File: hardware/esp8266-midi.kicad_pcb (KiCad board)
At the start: 2 copper layers, 60.1 x 63.5 mm, 26 parts, among them J1 MIDI in, J2 MIDI out, J3 TTL-232R-3V3 connector, J4 Bat+, J5 Bat-, SW1 reset, SW2 prog enable, U1 ESP-12E, U2 6N138, U3 LD1117S50TR_SOT223

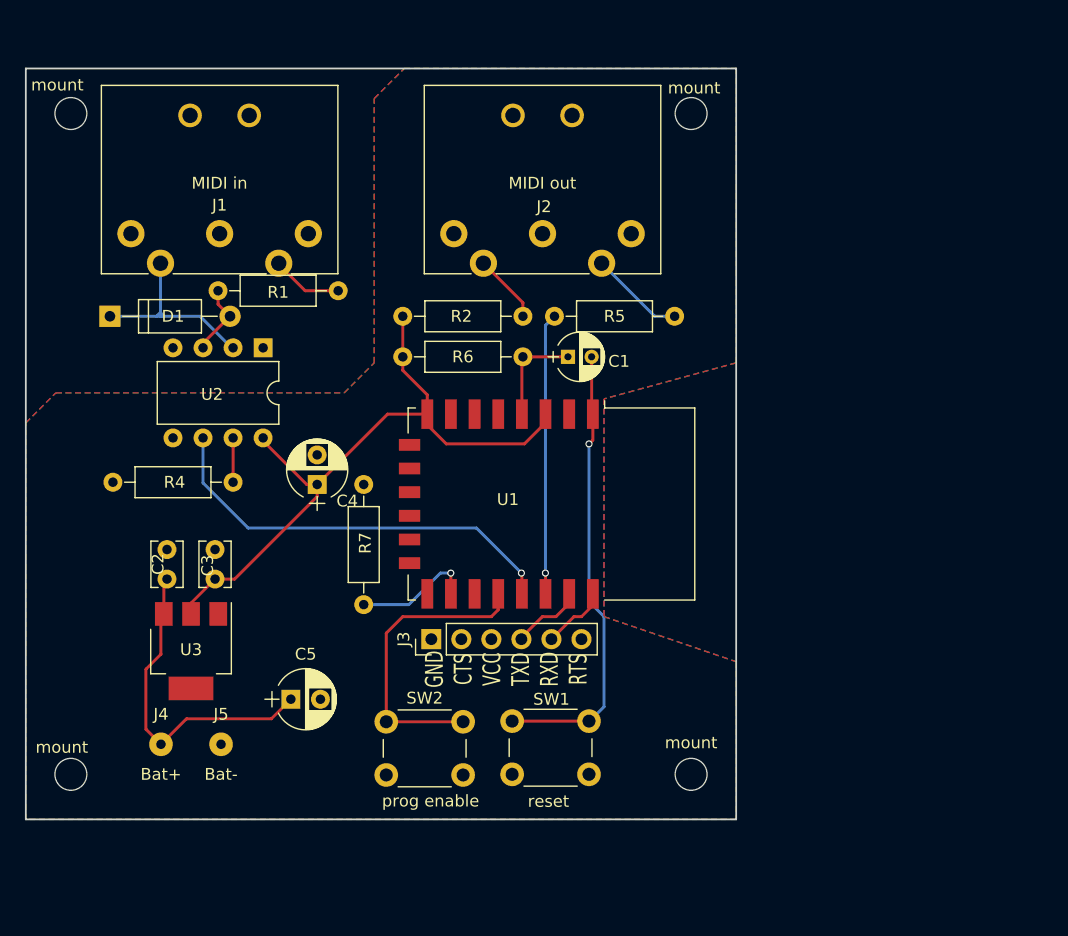
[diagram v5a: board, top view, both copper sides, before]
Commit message: New layout with (mostly) smd components, pcb shaped for CRDCGG003 enclosure
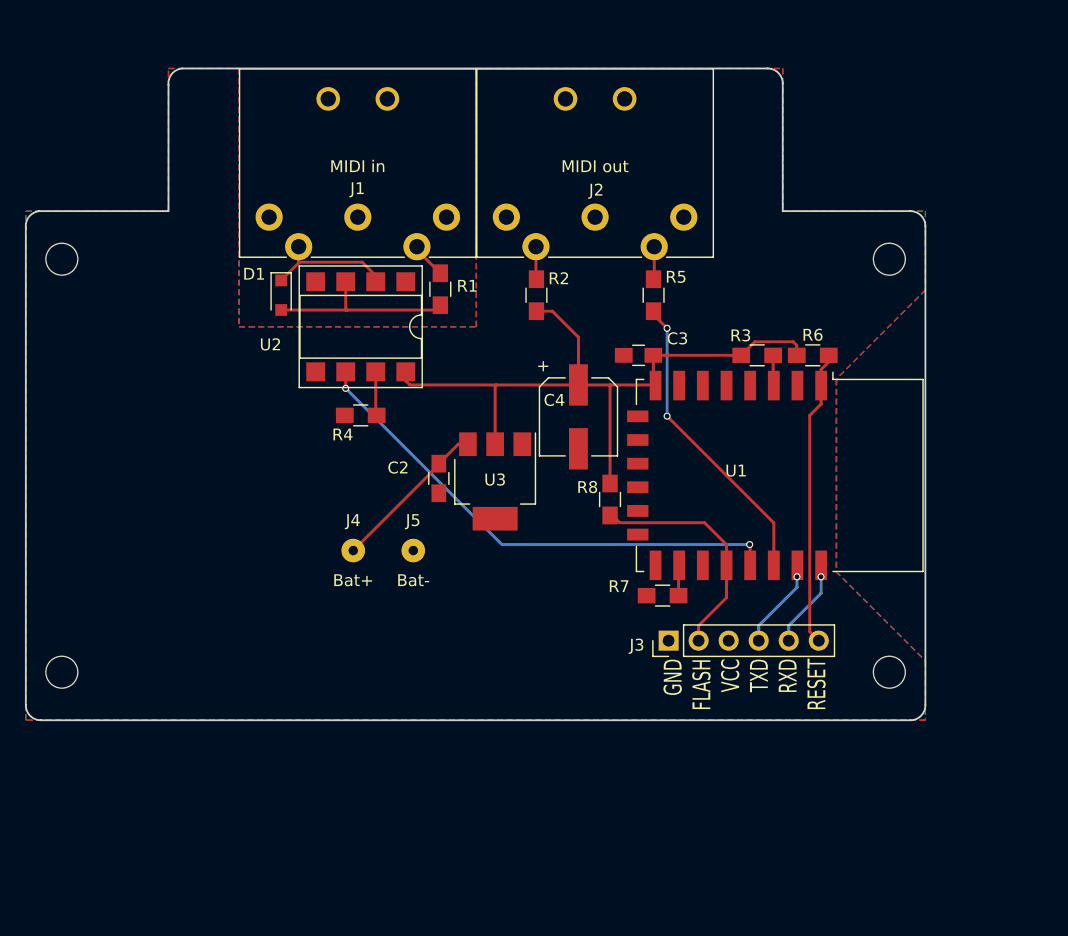
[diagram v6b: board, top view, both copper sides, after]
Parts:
- removed C1: 1uF, Capacitors_THT:CP_Radial_D4.0mm_P2.00mm
- removed C5: 220uF, Capacitors_THT:CP_Radial_D5.0mm_P2.50mm
- removed SW1: reset, Buttons_Switches_THT:SW_PUSH_6mm
- removed SW2: prog enable, Buttons_Switches_THT:SW_PUSH_6mm
- removed mount (x4): M2.5, Mounting_Holes:MountingHole_2.7mm_M2.5
- added ?: , Mounting_Holes:MountingHole_2.7mm_M2.5, F.Cu at (178.4, 120.3)
- added ?: , Mounting_Holes:MountingHole_2.7mm_M2.5, F.Cu at (178.4, 85.3)
- added ?: , Mounting_Holes:MountingHole_2.7mm_M2.5, F.Cu at (108.5, 120.3)
- added ?: , Mounting_Holes:MountingHole_2.7mm_M2.5, F.Cu at (108.5, 85.3)
- added R3: 10K, Resistors_SMD:R_0805_HandSoldering, F.Cu at (167.3, 93.5)
- added R8: 10K, Resistors_SMD:R_0805_HandSoldering, F.Cu at (154.8, 105.7)
- C2, C3: footprint Capacitors_THT:C_Disc_D3.8mm_W2.6mm_P2.50mm -> Capacitors_SMD:C_0805_HandSoldering
- C4: footprint Capacitors_THT:CP_Radial_D5.0mm_P2.50mm -> Capacitors_SMD:CP_Elec_6.3x5.8
- D1: footprint Diodes_THT:D_A-405_P10.16mm_Horizontal -> Diodes_SMD:D_SOD-323_HandSoldering
- R1, R2, R4, R5, R7: footprint Resistors_THT:R_Axial_DIN0207_L6.3mm_D2.5mm_P10.16mm_Horizontal -> Resistors_SMD:R_0805_HandSoldering
- R6: value 1K -> 10K; footprint Resistors_THT:R_Axial_DIN0207_L6.3mm_D2.5mm_P10.16mm_Horizontal -> Resistors_SMD:R_0805_HandSoldering
- U2: footprint Housings_DIP:DIP-8_W7.62mm -> Housings_DIP:DIP-8_W7.62mm_SMDSocket_SmallPads
- U3: value LD1117S50TR_SOT223 -> LD1117S50TR
- moved C3 40.5 mm to (157.2, 93.5), turned to 180 degrees
- moved R6 34.7 mm to (172.0, 93.5)
- moved U3 29.5 mm to (145.1, 104.1)
- moved R7 25.3 mm to (159.3, 113.8), turned to 180 degrees
- moved C2 24.5 mm to (140.3, 103.9), turned to 270 degrees
- moved J4 23.1 mm to (133.1, 110.0)
- moved J5 23.1 mm to (138.2, 110.0)
- moved C4 22.8 mm to (152.1, 98.7), turned to 270 degrees
- moved R4 21.7 mm to (133.7, 98.6)
- moved J3 20.1 mm to (159.8, 117.6)
- moved U1 19.5 mm to (169.2, 103.6)
- moved D1 14.6 mm to (127.0, 88.4), turned to 270 degrees
- moved J1 11.8 mm to (126.0, 81.8)
- moved R1 8.64 mm to (140.5, 87.9), turned to 270 degrees
- moved R5 8.57 mm to (158.5, 88.4), turned to 90 degrees
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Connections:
- J3 pad 2: (no net) -> Net-(J3-Pad2)
- J3 pad 6: (no net) -> Net-(J3-Pad6)
- R6 pad 2: Net-(C1-Pad1) -> Net-(J3-Pad6)
- U1 pad 1: Net-(C1-Pad2) -> Net-(J3-Pad6)
- U1 pad 18: Net-(SW2-Pad1) -> Net-(J3-Pad2)
- U1 pad 3: +3V3 -> Net-(R3-Pad1)
- U1 pad 4: Net-(C1-Pad1) -> (no net)
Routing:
- net Net-(C1-Pad2): track 38.9 -> 0.00 mm, vias 1 -> 0
- net Net-(SW2-Pad1): track 25.6 -> 0.00 mm
- net Net-(J3-Pad6): track 0.00 -> 25.1 mm
- net Net-(J3-Pad2): track 0.00 -> 20.0 mm
- net Net-(C2-Pad1): track 27.8 -> 13.6 mm
- net Net-(D1-Pad2): track 6.19 -> 16.2 mm
- net Net-(C1-Pad1): track 8.69 -> 0.00 mm
- net Net-(R7-Pad1): track 10.9 -> 3.24 mm, vias 1 -> 0
- net Net-(U1-Pad19): track 35.7 -> 42.8 mm, vias 1 -> 2
- net Net-(D1-Pad1): track 17.3 -> 11.0 mm
- net Net-(J2-Pad5): track 8.03 -> 2.78 mm
- net +3V3: track 58.3 -> 61.5 mm
- net Net-(J2-Pad4): track 5.87 -> 2.77 mm
- net Net-(J1-Pad5): track 6.04 -> 3.07 mm
- net Net-(R3-Pad1): track 0.00 -> 2.58 mm
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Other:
- board size 60.1 x 63.5 mm -> 76.1 x 55.1 mm
- board text added: "GND FLASH VCC TXD RXD RESET"
- board text removed: "GND CTS VCC TXD RXD RTS"

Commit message: Kicad5: pcb after converting to kicad5
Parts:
- U3: value LD1117S50TR -> LD1117S50TR_SOT223
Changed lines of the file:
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@@
-(kicad_pcb (version 4) (host pcbnew 4.0.7-e2-6376~58~ubuntu14.04.1)
+(kicad_pcb (version 20171130) (host pcbnew 5.0.1-33cea8e~68~ubuntu18.04.1)
   (general
-    (links 38)
-    (no_connects 0)
-    (area 105.328665 69.139999 181.558001 124.408001)
     (thickness 1.6)
     (drawings 23)
@@
     (pad_drill 0.762)
     (pad_to_mask_clearance 0.2)
+    (solder_mask_min_width 0.25)
     (aux_axis_origin 0 0)
     (visible_elements FFFFFF7F)
@@
       (layerselection 0x00030_80000001)
       (usegerberextensions false)
+      (usegerberattributes false)
+      (usegerberadvancedattributes false)
+      (creategerberjobfile false)
       (excludeedgelayer true)
       (linewidth 0.100000)
@@
       (hpglpennumber 1)
       (hpglpenspeed 20)
-      (hpglpendiameter 15)
-      (hpglpenoverlay 2)
+      (hpglpendiameter 15.000000)
       (psnegative false)
       (psa4output false)
@@
     (tags "Wi-Fi Module")
     (attr smd)
-    (fp_text reference U1 (at -0.381 3.683 360) (layer F.SilkS)
-      (effects (font (size 1 1) (thickness 0.15)))
-    )
-    (fp_text value ESP-12E (at -2.286 3.683 360) (layer F.Fab)
-      (effects (font (size 1 1) (thickness 0.15)))
-    )
-    (fp_text user Antenna (at -0.06 -7 450) (layer Cmts.User)
-      (effects (font (size 1 1) (thickness 0.15)))
-    )
-    (fp_text user "KEEP-OUT ZONE" (at 0.03 -9.55 450) (layer Cmts.User)
+    (fp_text reference U1 (at -0.381 3.683) (layer F.SilkS)
+      (effects (font (size 1 1) (thickness 0.15)))
+    )
+    (fp_text value ESP-12E (at -2.286 3.683) (layer F.Fab)
+      (effects (font (size 1 1) (thickness 0.15)))
+    )
+    (fp_text user Antenna (at -0.06 -7 90) (layer Cmts.User)
+      (effects (font (size 1 1) (thickness 0.15)))
+    )
+    (fp_text user "KEEP-OUT ZONE" (at 0.03 -9.55 90) (layer Cmts.User)
       (effects (font (size 1 1) (thickness 0.15)))
     )
@@
     (pad "" thru_hole circle (at 10 -10) (size 2 2) (drill 1.3) (layers *.Cu *.Mask))
     (model ${KISYS3DMOD}/Connectors.3dshapes/SDS-50J.wrl
-      (at (xyz 0.29 0.49 0))
+      (offset (xyz 7.365999889373779 12.44599981307983 0))
       (scale (xyz 0.39 0.39 0.39))
       (rotate (xyz -90 0 180))
@@
     (pad "" thru_hole circle (at 10 -10) (size 2 2) (drill 1.3) (layers *.Cu *.Mask))
     (model ${KISYS3DMOD}/Connectors.3dshapes/SDS-50J.wrl
-      (at (xyz 0.29 0.49 0))
+      (offset (xyz 7.365999889373779 12.44599981307983 0))
       (scale (xyz 0.39 0.39 0.39))
       (rotate (xyz -90 0 180))
@@
     (tags "CMS SOT")
     (attr smd)
-    (fp_text reference U3 (at -0.127 0 360) (layer F.SilkS)
-      (effects (font (size 1 1) (thickness 0.15)))
-    )
-    (fp_text value LD1117S50TR (at 6.35 -0.9525 360) (layer F.Fab)
-      (effects (font (size 1 1) (thickness 0.15)))
-    )
-    (fp_text user %R (at 0 0 360) (layer F.Fab)
+    (fp_text reference U3 (at -0.127 0) (layer F.SilkS)
+      (effects (font (size 1 1) (thickness 0.15)))
+    )
+    (fp_text value LD1117S50TR_SOT223 (at 6.35 -0.9525) (layer F.Fab)
+      (effects (font (size 1 1) (thickness 0.15)))
+    )
+    (fp_text user %R (at 0 0) (layer F.Fab)
       (effects (font (size 0.8 0.8) (thickness 0.12)))
     )
@@
     (tags "capacitor 0805")
     (attr smd)
-    (fp_text reference C2 (at -0.889 3.429 360) (layer F.SilkS)
-      (effects (font (size 1 1) (thickness 0.15)))
-    )
-    (fp_text value 100nF (at 0.762 3.302 360) (layer F.Fab)
+    (fp_text reference C2 (at -0.889 3.429) (layer F.SilkS)
+      (effects (font (size 1 1) (thickness 0.15)))
+    )
+    (fp_text value 100nF (at 0.762 3.302) (layer F.Fab)
       (effects (font (size 1 1) (thickness 0.15)))
     )
@@
     (descr "SMT capacitor, aluminium electrolytic, 6.3x5.8")
     (attr smd)
-    (fp_text reference C4 (at -1.397 2.032 360) (layer F.SilkS)
-      (effects (font (size 1 1) (thickness 0.15)))
-    )
-    (fp_text value 220uF (at 0.127 -0.254 360) (layer F.Fab)
+    (fp_text reference C4 (at -1.397 2.032) (layer F.SilkS)
+      (effects (font (size 1 1) (thickness 0.15)))
+    )
+    (fp_text value 220uF (at 0.127 -0.254) (layer F.Fab)
       (effects (font (size 1 1) (thickness 0.15)))
     )
@@
     (tags SOD-323)
     (attr smd)
-    (fp_text reference D1 (at -1.778 2.286 360) (layer F.SilkS)
-      (effects (font (size 1 1) (thickness 0.15)))
-    )
-    (fp_text value 1N4148 (at -0.127 4.318 360) (layer F.Fab)
+    (fp_text reference D1 (at -1.778 2.286) (layer F.SilkS)
+      (effects (font (size 1 1) (thickness 0.15)))
+    )
+    (fp_text value 1N4148 (at -0.127 4.318) (layer F.Fab)
       (effects (font (size 1 1) (thickness 0.15)))
     )
@@
     (tags "resistor 0805")
     (attr smd)
-    (fp_text reference R1 (at -0.254 -2.286 360) (layer F.SilkS)
-      (effects (font (size 1 1) (thickness 0.15)))
-    )
-    (fp_text value 220R (at -1.8415 -2.921 360) (layer F.Fab)
+    (fp_text reference R1 (at -0.254 -2.286) (layer F.SilkS)
+      (effects (font (size 1 1) (thickness 0.15)))
+    )
+    (fp_text value 220R (at -1.8415 -2.921) (layer F.Fab)
       (effects (font (size 1 1) (thickness 0.15)))
     )
@@
     (tags "resistor 0805")
     (attr smd)
-    (fp_text reference R2 (at -1.397 -1.905 360) (layer F.SilkS)
-      (effects (font (size 1 1) (thickness 0.15)))
-    )
-    (fp_text value 120R (at 0 -3.048 360) (layer F.Fab)
+    (fp_text reference R2 (at -1.397 -1.905) (layer F.SilkS)
+      (effects (font (size 1 1) (thickness 0.15)))
+    )
+    (fp_text value 120R (at 0 -3.048) (layer F.Fab)
       (effects (font (size 1 1) (thickness 0.15)))
     )
@@
     (tags "THT DIP DIL PDIP 2.54mm 7.62mm 300mil SMDSocket SmallPads")
     (attr smd)
-    (fp_text reference U2 (at 1.524 7.62 360) (layer F.SilkS)
-      (effects (font (size 1 1) (thickness 0.15)))
-    )
-    (fp_text value 6N138 (at 3.048 7.747 360) (layer F.Fab)
-      (effects (font (size 1 1) (thickness 0.15)))
-    )
+    (fp_text reference U2 (at 1.524 7.62) (layer F.SilkS)
+      (effects (font (size 1 1) (thickness 0.15)))
+    )
+    (fp_text value 6N138 (at 3.048 7.747) (layer F.Fab)
+      (effects (font (size 1 1) (thickness 0.15)))
+    )

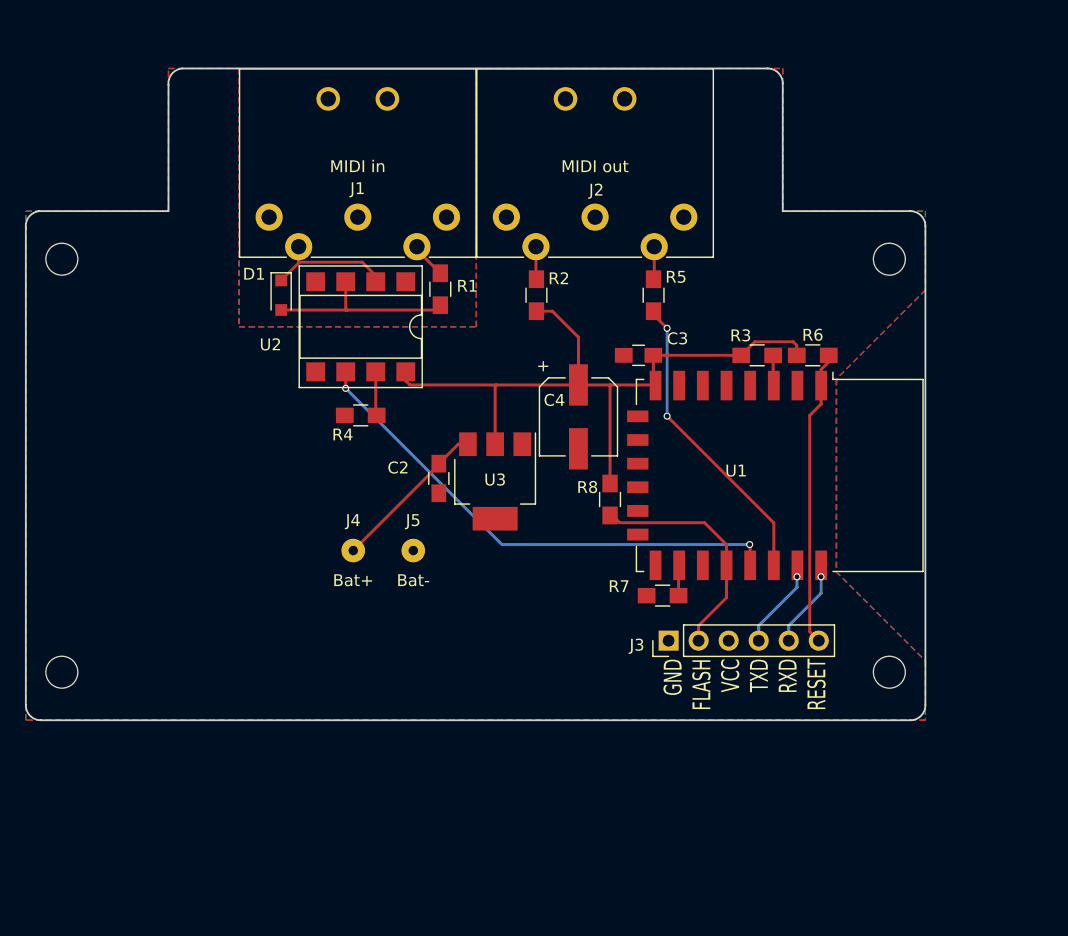
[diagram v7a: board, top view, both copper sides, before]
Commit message: Updated PCB with new components .. little questionable / not final.
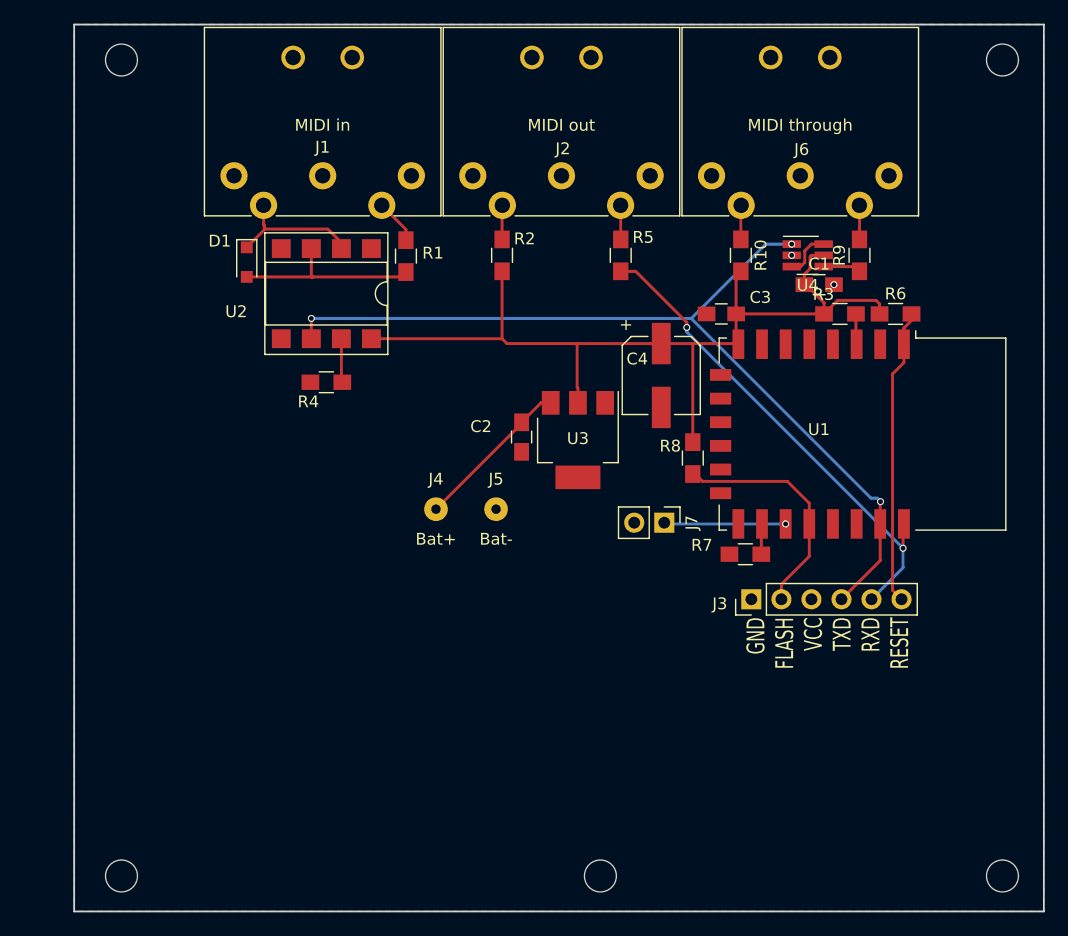
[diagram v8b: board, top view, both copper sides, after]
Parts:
- removed the ? at (178.4, 120.3)
- removed the ? at (178.4, 85.3)
- removed the ? at (108.5, 120.3)
- removed the ? at (108.5, 85.3)
- added ?: , Mounting_Holes:MountingHole_2.7mm_M2.5, F.Cu at (154.0, 137.5)
- added ?: , Mounting_Holes:MountingHole_2.7mm_M2.5, F.Cu at (188.0, 137.5)
- added ?: , Mounting_Holes:MountingHole_2.7mm_M2.5, F.Cu at (113.5, 137.5)
- added ?: , Mounting_Holes:MountingHole_2.7mm_M2.5, F.Cu at (188.0, 68.5)
- added ?: , Mounting_Holes:MountingHole_2.7mm_M2.5, F.Cu at (113.5, 68.5)
- added C1: 100nF, Capacitors_SMD:C_0805_HandSoldering, F.Cu at (172.5, 87.5)
- added J6: MIDI through, Connectors:SDS-50J, F.Cu at (163.4, 78.3)
- added J7: Debug serial out, Pin_Headers:Pin_Header_Straight_1x02_Pitch2.54mm, F.Cu at (159.4, 107.6)
- added R10: 120R, Resistors_SMD:R_0805_HandSoldering, F.Cu at (165.9, 85.0)
- added R9: 120R, Resistors_SMD:R_0805_HandSoldering, F.Cu at (175.9, 85.0)
- added U4: 74LVC2G14, TO_SOT_Packages_SMD:SOT-23-6_Handsoldering, F.Cu at (171.5, 85.0)
- moved C2 7.83 mm to (147.3, 100.4)
- moved C3 7.83 mm to (164.2, 90.0)
- moved C4 7.83 mm to (159.1, 95.2)
- moved J3 7.83 mm to (166.8, 114.1)
- moved J4 7.83 mm to (140.1, 106.5)
- moved J5 7.83 mm to (145.2, 106.5)
- moved R3 7.83 mm to (174.3, 90.0)
- moved R6 7.83 mm to (179.0, 90.0)
- moved R7 7.83 mm to (166.3, 110.3)
- moved R8 7.83 mm to (161.8, 102.2)
- moved U1 7.83 mm to (176.2, 100.1)
- moved U3 7.83 mm to (152.1, 100.6)
- moved J1 4.59 mm to (123.0, 78.3)
- moved J2 4.51 mm to (143.2, 78.3)
- moved R2 4.45 mm to (145.7, 85.0)
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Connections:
- net +3V3 renamed VCC
- J3 pad 4: Net-(J3-Pad4) -> UART0_RXD
- J3 pad 5: Net-(J3-Pad5) -> UART0_TXD
- R5 pad 1: Net-(R5-Pad1) -> UART0_TXD
- U1 pad 17: (no net) -> Net-(J7-Pad1)
- U1 pad 19: Net-(U1-Pad19) -> (no net)
- U1 pad 20: Net-(R5-Pad1) -> (no net)
- U1 pad 21: Net-(J3-Pad4) -> UART0_RXD
- U1 pad 22: Net-(J3-Pad5) -> UART0_TXD
- U2 pad 6: Net-(U1-Pad19) -> UART0_RXD
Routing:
- net UART0_RXD: track 0.00 -> 77.1 mm, vias 0 -> 3
- net Net-(U1-Pad19): track 42.8 -> 0.00 mm, vias 2 -> 0
- net UART0_TXD: track 0.00 -> 41.6 mm, vias 0 -> 2
- net Net-(R5-Pad1): track 25.7 -> 0.00 mm, vias 2 -> 0
- net VCC: track 61.5 -> 78.6 mm
- net Net-(J7-Pad1): track 0.00 -> 10.3 mm, vias 0 -> 1
- net Net-(J3-Pad4): track 7.73 -> 0.00 mm, vias 1 -> 0
- net Net-(J3-Pad5): track 7.50 -> 0.00 mm, vias 1 -> 0
- net Net-(U4-Pad3): track 0.00 -> 4.06 mm
- net Net-(R9-Pad1): track 0.00 -> 3.20 mm
- net Net-(J6-Pad4): track 0.00 -> 2.89 mm
- net Net-(J6-Pad5): track 0.00 -> 2.88 mm
- net Net-(J1-Pad5): track 3.07 -> 3.79 mm
- net Net-(D1-Pad1): track 11.0 -> 11.6 mm
- net GND: vias 0 -> 2
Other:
- board size 76.1 x 55.1 mm -> 82 x 75 mm
